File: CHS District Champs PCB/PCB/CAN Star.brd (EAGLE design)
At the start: 62.3 x 55.6 mm, 14 parts

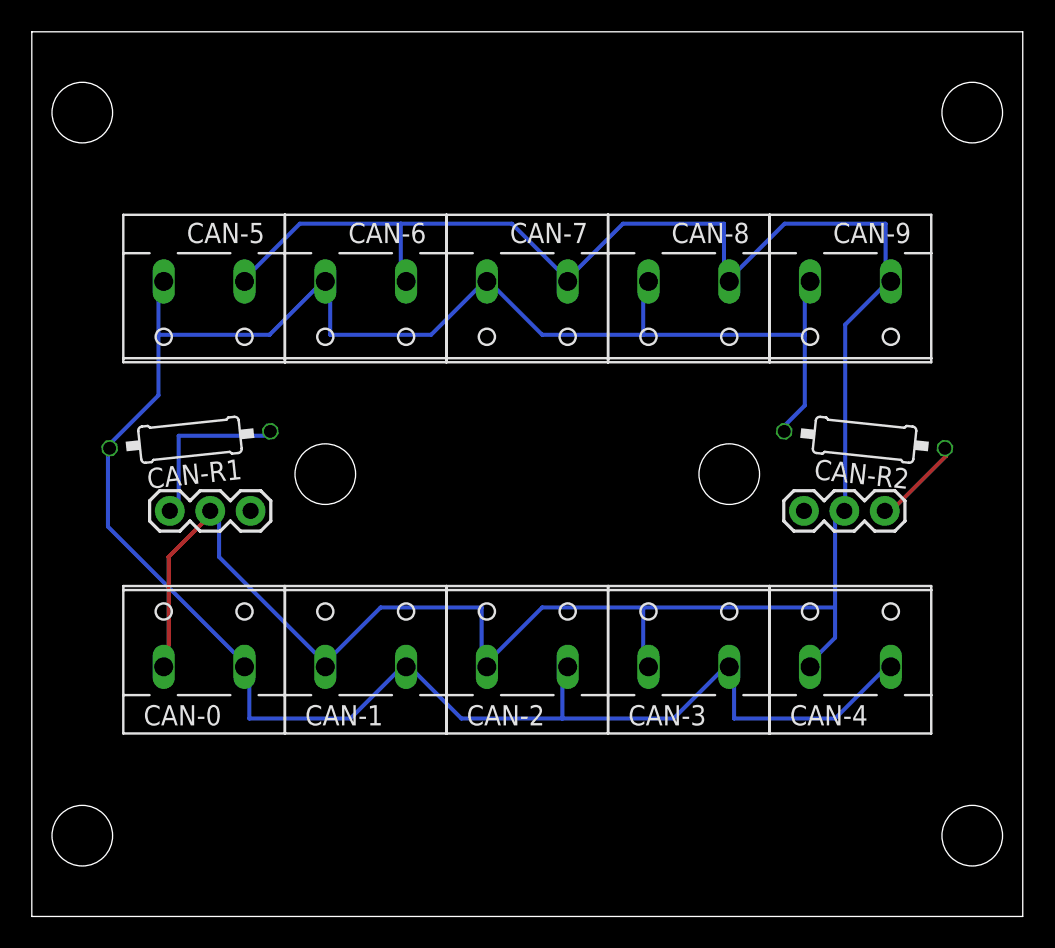
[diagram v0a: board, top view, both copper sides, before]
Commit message: Updated with finalized files for District Champs PCB Gift, including a new holder stl and image, along with a smaller board with the url on it eagle files and image.
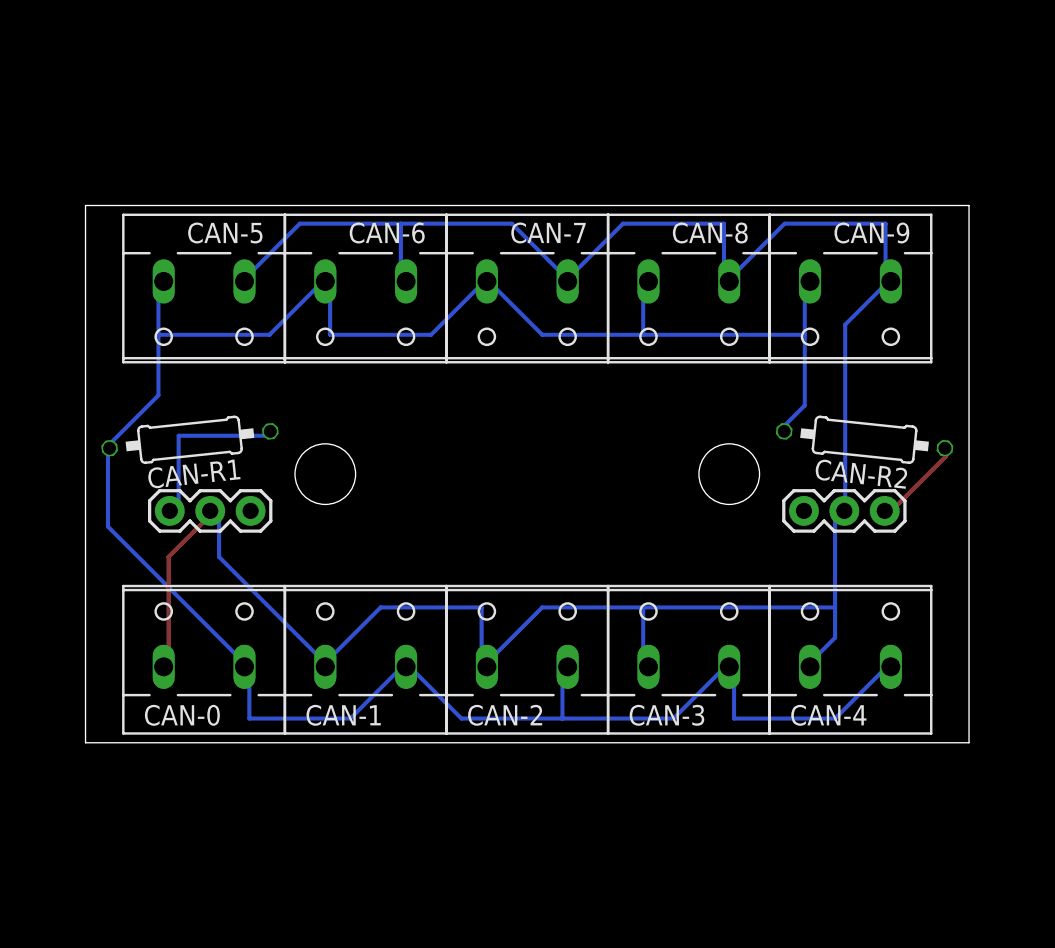
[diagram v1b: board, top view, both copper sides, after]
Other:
- board size 62.3 x 55.6 mm -> 55.6 x 33.8 mm
- board text added: "RoboLoCo Team 5338 goo.gl/W5tM8y"
- board text removed: "RoboLoCo Team 5338"
- board text removed: "Star Board v7"
- board text removed: "http://team5338.org"
- board text removed: "https://tinyurl.com/5338-PCBs"
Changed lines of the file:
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@@
 <layer number="18" name="Vias" color="2" fill="1" visible="yes" active="yes"/>
 <layer number="19" name="Unrouted" color="6" fill="1" visible="yes" active="yes"/>
-<layer number="20" name="Dimension" color="24" fill="1" visible="no" active="yes"/>
+<layer number="20" name="Dimension" color="24" fill="1" visible="yes" active="yes"/>
 <layer number="21" name="tPlace" color="7" fill="1" visible="yes" active="yes"/>
 <layer number="22" name="bPlace" color="7" fill="1" visible="no" active="yes"/>
-<layer number="23" name="tOrigins" color="15" fill="1" visible="no" active="yes"/>
+<layer number="23" name="tOrigins" color="15" fill="1" visible="yes" active="yes"/>
 <layer number="24" name="bOrigins" color="15" fill="1" visible="no" active="yes"/>
 <layer number="25" name="tNames" color="7" fill="1" visible="yes" active="yes"/>
@@
 <layer number="42" name="bRestrict" color="1" fill="10" visible="yes" active="yes"/>
 <layer number="43" name="vRestrict" color="2" fill="10" visible="yes" active="yes"/>
-<layer number="44" name="Drills" color="7" fill="1" visible="no" active="yes"/>
-<layer number="45" name="Holes" color="7" fill="1" visible="no" active="yes"/>
+<layer number="44" name="Drills" color="7" fill="1" visible="yes" active="yes"/>
+<layer number="45" name="Holes" color="7" fill="1" visible="yes" active="yes"/>
 <layer number="46" name="Milling" color="3" fill="1" visible="no" active="yes"/>
 <layer number="47" name="Measures" color="7" fill="1" visible="no" active="yes"/>
@@
 <fusionsync huburn="a.cGVyc29uYWw6dWUyOTkyNzlm" projecturn="a.cGVyc29uYWw6dWUyOTkyNzlmIzIwMTcxMTMwMTA2NDg0MTMx" f3durn="urn:adsk.wipprod:dm.lineage:8Aa422irTc--NrJX5DtlpQ" pcbguid="517755bc-c0e1-4e1b-a016-5347d8e8e154" lastpulledtime="" lastsyncedchangeguid="ef4b0037-dd61-dc77-918d-7c4fdb6cf8c6"/>
 <plain>
-<wire x1="-5.42416875" y1="-12.446" x2="56.88456875" y2="-12.446" width="0" layer="20"/>
-<wire x1="56.88456875" y1="-12.446" x2="56.88456875" y2="43.18" width="0" layer="20"/>
-<wire x1="56.88456875" y1="43.18" x2="-5.42416875" y2="43.18" width="0" layer="20"/>
-<wire x1="-5.42416875" y1="43.18" x2="-5.42416875" y2="-12.446" width="0" layer="20"/>
+<wire x1="-2.04596875" y1="-1.524" x2="53.50636875" y2="-1.524" width="0" layer="20"/>
+<wire x1="53.50636875" y1="-1.524" x2="53.50636875" y2="32.258" width="0" layer="20"/>
+<wire x1="53.50636875" y1="32.258" x2="-2.04596875" y2="32.258" width="0" layer="20"/>
+<wire x1="-2.04596875" y1="32.258" x2="-2.04596875" y2="-1.524" width="0" layer="20"/>
 <hole x="13.0302" y="15.367" drill="3.81" locked="yes"/>
 <hole x="38.4302" y="15.367" drill="3.81" locked="yes"/>
-<text x="25.7302" y="16.2814" size="1.651" layer="27" font="vector" ratio="10" align="center">RoboLoCo
-Team 5338</text>
-<text x="25.7302" y="12.954" size="1.524" layer="27" font="vector" ratio="10" align="center">Star Board v7</text>
+<text x="25.7302" y="15.367" size="1.524" layer="27" font="vector" ratio="10" align="center">RoboLoCo
+Team 5338
+goo.gl/W5tM8y</text>
 <text x="2.8702" y="19.939" size="1.27" layer="27" font="vector" ratio="10" align="center">Y(H)</text>
 <text x="7.9502" y="19.939" size="1.27" layer="27" font="vector" ratio="10" align="center">G(L)</text>
@@
 <text x="0.737615625" y="13.0556" size="1.27" layer="27" font="vector" ratio="10" align="center">ON</text>
 <text x="51.0032" y="13.0556" size="1.27" layer="27" font="vector" ratio="10" align="center">ON</text>
-<hole x="-2.249425" y="38.1" drill="3.81"/>
-<hole x="-2.249425" y="-7.366" drill="3.81"/>
-<hole x="53.709825" y="38.1" drill="3.81"/>
-<hole x="53.709825" y="-7.366" drill="3.81"/>
-<text x="25.7302" y="-7.366" size="2.032" layer="27" font="vector" ratio="10" align="center">https://tinyurl.com/5338-PCBs</text>
-<text x="25.7302" y="38.1" size="2.032" layer="27" font="vector" ratio="10" align="center">http://team5338.org</text>
 </plain>
 <attributes>
@@
 </signal>
 </signals>
-<errors>
-</errors>
 </board>
 </drawing>
